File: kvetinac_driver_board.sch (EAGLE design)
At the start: 150 parts, among them IC1 MEGA128-A, IC3 74HC238D, IC4 VNH2SP30, IC5 VNH2SP30, J1 PINHD-1X1SMD2.4MM, J10 PINHD-1X1SMD2.4MM, J11 PINHD-1X1SMD2.4MM, J12 PINHD-1X1SMD2.4MM, J13 PINHD-1X1SMD2.4MM, J14 PINHD-1X1SMD2.4MM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

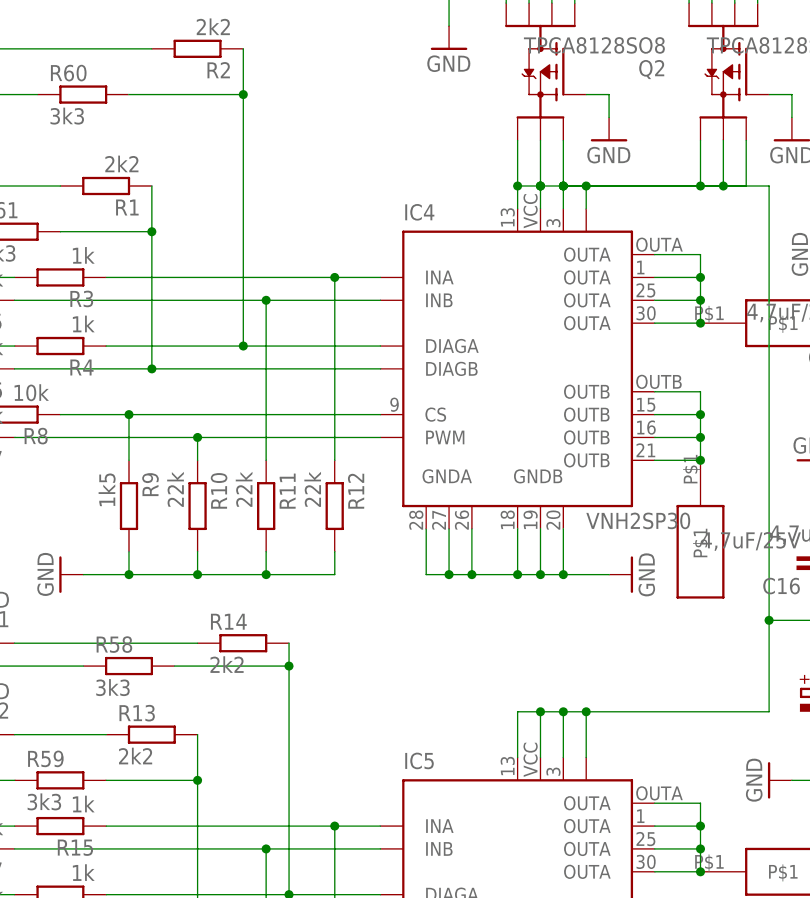
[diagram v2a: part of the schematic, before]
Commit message: Nov? verze: Upraveny plosky pod drivery VNH2SP30. Pridany vie pod drivery VNH2SP30 - kvuli umozneni pripajeni z druhe strany.
Upraven DESCRIPTION:
Pridany INSTRUKCE PRO VYROBU a pro PRVNI OZIVENI DESKY.
Popsany vsechny veci kolem desky a jeji vyroby.
VSICHNI POVINNE PROCIST!!!
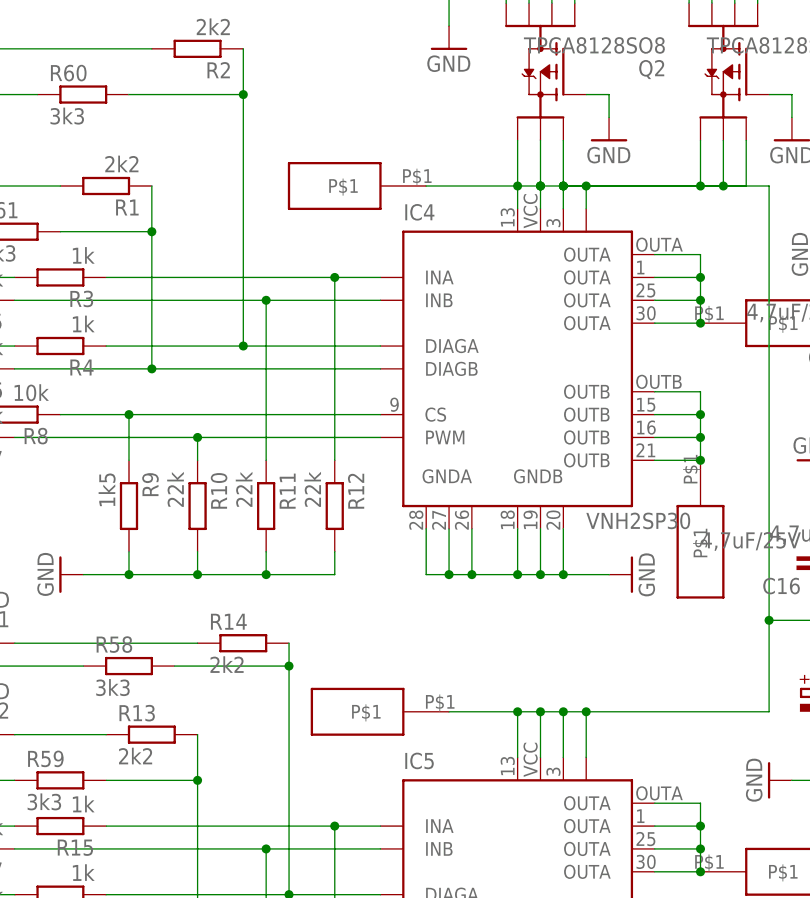
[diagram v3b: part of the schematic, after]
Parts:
- added VCCA, VCCB: CABEL_SMDCABEL_SMD_12*6MM, cabel_smd:CABEL_SMDCABEL_SMD_12*6MM
- OUTA_1, OUTA_2, OUTB_1, OUTB_2: value CABEL_SMD -> CABEL_SMDCABEL_SMD_6.5*6MM; device cabel_smd:CABEL_SMD -> cabel_smd:CABEL_SMDCABEL_SMD_6.5*6MM
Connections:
- net VCC: now also VCCA.P$1, VCCB.P$1
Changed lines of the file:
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@@
 <?xml version="1.0" encoding="utf-8"?>
 <!DOCTYPE eagle SYSTEM "eagle.dtd">
-<eagle version="6.1">
+<eagle version="6.3">
 <drawing>
 <settings>
@@
 <part name="VCC" library="cabel_smd" deviceset="CABEL_SMD" device=""/>
 <part name="0V" library="cabel_smd" deviceset="CABEL_SMD" device=""/>
-<part name="OUTB_2" library="cabel_smd" deviceset="CABEL_SMD" device=""/>
-<part name="OUTA_2" library="cabel_smd" deviceset="CABEL_SMD" device=""/>
-<part name="OUTA_1" library="cabel_smd" deviceset="CABEL_SMD" device=""/>
-<part name="OUTB_1" library="cabel_smd" deviceset="CABEL_SMD" device=""/>
+<part name="OUTB_2" library="cabel_smd" deviceset="CABEL_SMD" device="CABEL_SMD_6.5*6MM" value="CABEL_SMDCABEL_SMD_6.5*6MM"/>
+<part name="OUTA_2" library="cabel_smd" deviceset="CABEL_SMD" device="CABEL_SMD_6.5*6MM" value="CABEL_SMDCABEL_SMD_6.5*6MM"/>
+<part name="OUTA_1" library="cabel_smd" deviceset="CABEL_SMD" device="CABEL_SMD_6.5*6MM" value="CABEL_SMDCABEL_SMD_6.5*6MM"/>
+<part name="OUTB_1" library="cabel_smd" deviceset="CABEL_SMD" device="CABEL_SMD_6.5*6MM" value="CABEL_SMDCABEL_SMD_6.5*6MM"/>
 <part name="PG2_CON" library="pinhead" deviceset="PINHD-1X2" device=""/>
 <part name="R72" library="rcl" deviceset="R-EU_" device="R0603" value="220"/>
@@
 <part name="GND5" library="supply1" deviceset="GND" device=""/>
 <part name="C23" library="rcl_upravena" deviceset="C-EU" device="C0306" value="100nF/6,3V"/>
+<part name="VCCB" library="cabel_smd" deviceset="CABEL_SMD" device="CABEL_SMD_12*6MM"/>
+<part name="VCCA" library="cabel_smd" deviceset="CABEL_SMD" device="CABEL_SMD_12*6MM"/>
 </parts>
 <sheets>
@@
 <instance part="GND5" gate="1" x="93.98" y="83.82"/>
 <instance part="C23" gate="G$1" x="58.42" y="-78.74"/>
+<instance part="VCCB" gate="G$1" x="68.58" y="78.74" rot="R180"/>
+<instance part="VCCA" gate="G$1" x="71.12" y="20.32" rot="R180"/>
 </instances>
 <busses>
@@
 <pinref part="IC5" gate="G$1" pin="VCC"/>
 <pinref part="IC5" gate="G$1" pin="VCC@2"/>
-</segment>
-</net>
+<pinref part="VCCB" gate="G$1" pin="P$1"/>
+<wire x1="73.66" y1="78.74" x2="83.82" y2="78.74" width="0.1524" layer="91"/>
+<pinref part="VCCA" gate="G$1" pin="P$1"/>
+<wire x1="76.2" y1="20.32" x2="83.82" y2="20.32" width="0.1524" layer="91"/>
+<junction x="83.82" y="20.32"/>
+</segment>
+</net>
